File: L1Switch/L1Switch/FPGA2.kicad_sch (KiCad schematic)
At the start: 43 parts, among them J10 Conn_02x07_Odd_Even, U1 XC7A35T-FTG256, U10 W25Q128JVS, U11 TXB0108PW, U12 TPS386000RGPR

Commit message: Update part numbers.
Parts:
- C376, C377: MFR Part# GRM155R71C104KA57D -> GRM155R71C104KA88D
- R256, R257, R258: MFR Part# (none) -> RC0402FR-132KL; Manufacturer (none) -> Yageo
- R259: MFR Part# (none) -> RC0402FR-074K7L; Manufacturer (none) -> Yageo
- R260: MFR Part# (none) -> RC0402FR-0768K1L; Manufacturer (none) -> Yageo
- R261, R263, R265, R268: MFR Part# (none) -> CRCW040210K0FKED; Manufacturer (none) -> Vishay
- R262: MFR Part# (none) -> RC0402FR-0732K4L; Manufacturer (none) -> Yageo
- R264: MFR Part# (none) -> RC0402FR-0718K7L; Manufacturer (none) -> Yageo
- R266: MFR Part# (none) -> RC0402FR-0714K3L; Manufacturer (none) -> Yageo
- R267: MFR Part# (none) -> RC0402FR-071K1L; Manufacturer (none) -> Yageo
- R269: MFR Part# (none) -> RC0402FR-13100KL; Manufacturer (none) -> Yageo
- TP2, TP3, TP4: MFR Part# (none) -> -; Manufacturer (none) -> -
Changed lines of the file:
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@@
 (kicad_sch (version 20200608) (host eeschema "5.99.0-unknown-1973153~101~ubuntu20.04.1")
-  (page 3 12)
+  (page 1 12)
   (paper "B")
   (bus_alias "SPI_FLASH" (members "CS_N" "DI" "DO" "W_N" "HOLD_N"))
@@
   (junction (at 392.43 207.01))
   (junction (at 394.97 52.07))
-  (no_connect (at 233.68 120.65))
-  (no_connect (at 316.23 182.88))
+  (no_connect (at 233.68 138.43))
   (no_connect (at 367.03 148.59))
-  (no_connect (at 233.68 138.43))
   (no_connect (at 254 39.37))
   (no_connect (at 316.23 168.91))
+  (no_connect (at 316.23 182.88))
   (no_connect (at 254 41.91))
   (no_connect (at 233.68 123.19))
+  (no_connect (at 233.68 120.65))
   (no_connect (at 233.68 135.89))
   (bus_entry (at 347.98 49.53) (size -2.54 -2.54))
@@
       (effects (font (size 1.27 1.27)) hide)
     )
+    (property "MFR Part#" "-" (id 4) (at 242.57 105.41 0)
+      (effects (font (size 1.27 1.27)) hide)
+    )
+    (property "Manufacturer" "-" (id 5) (at 242.57 105.41 0)
+      (effects (font (size 1.27 1.27)) hide)
+    )
   )
   (symbol (lib_id "Connector:TestPoint") (at 256.54 113.03 180) (unit 1)
@@
       (effects (font (size 1.27 1.27)) hide)
     )
+    (property "MFR Part#" "-" (id 4) (at 256.54 113.03 0)
+      (effects (font (size 1.27 1.27)) hide)
+    )
+    (property "Manufacturer" "-" (id 5) (at 256.54 113.03 0)
+      (effects (font (size 1.27 1.27)) hide)
+    )
   )
   (symbol (lib_id "Connector:TestPoint") (at 379.73 127 0) (unit 1)
@@
     )
     (property "Datasheet" "~" (id 3) (at 384.81 127 0)
+      (effects (font (size 1.27 1.27)) hide)
+    )
+    (property "MFR Part#" "-" (id 4) (at 379.73 127 0)
+      (effects (font (size 1.27 1.27)) hide)
+    )
+    (property "Manufacturer" "-" (id 5) (at 379.73 127 0)
       (effects (font (size 1.27 1.27)) hide)
     )
@@
       (effects (font (size 1.27 1.27)) hide)
     )
+    (property "MFR Part#" "RC0402FR-074K7L" (id 4) (at 278.13 110.49 0)
+      (effects (font (size 1.27 1.27)) hide)
+    )
+    (property "Manufacturer" "Yageo" (id 5) (at 278.13 110.49 0)
+      (effects (font (size 1.27 1.27)) hide)
+    )
   )
   (symbol (lib_id "Device:R_US") (at 278.13 144.78 0) (unit 1)
@@
       (effects (font (size 1.27 1.27)) hide)
     )
+    (property "MFR Part#" "RC0402FR-0768K1L" (id 4) (at 278.13 144.78 0)
+      (effects (font (size 1.27 1.27)) hide)
+    )
+    (property "Manufacturer" "Yageo" (id 5) (at 278.13 144.78 0)
+      (effects (font (size 1.27 1.27)) hide)
+    )
   )
   (symbol (lib_id "Device:R_US") (at 278.13 184.15 0) (unit 1)
@@
       (effects (font (size 1.27 1.27)) hide)
     )
+    (property "MFR Part#" "CRCW040210K0FKED" (id 4) (at 278.13 184.15 0)
+      (effects (font (size 1.27 1.27)) hide)
+    )
+    (property "Manufacturer" "Vishay" (id 5) (at 278.13 184.15 0)
+      (effects (font (size 1.27 1.27)) hide)
+    )
   )
   (symbol (lib_id "Device:R_US") (at 288.29 144.78 0) (unit 1)
@@
       (effects (font (size 1.27 1.27)) hide)
     )
+    (property "MFR Part#" "RC0402FR-0732K4L" (id 4) (at 288.29 144.78 0)
+      (effects (font (size 1.27 1.27)) hide)
+    )
+    (property "Manufacturer" "Yageo" (id 5) (at 288.29 144.78 0)
+      (effects (font (size 1.27 1.27)) hide)
+    )
   )
   (symbol (lib_id "Device:R_US") (at 288.29 184.15 0) (unit 1)
@@
       (effects (font (size 1.27 1.27)) hide)
     )
+    (property "MFR Part#" "CRCW040210K0FKED" (id 4) (at 288.29 184.15 0)
+      (effects (font (size 1.27 1.27)) hide)
+    )
+    (property "Manufacturer" "Vishay" (id 5) (at 288.29 184.15 0)
+      (effects (font (size 1.27 1.27)) hide)
+    )
   )
   (symbol (lib_id "Device:R_US") (at 297.18 144.78 0) (unit 1)
@@
       (effects (font (size 1.27 1.27)) hide)
     )
+    (property "MFR Part#" "RC0402FR-0718K7L" (id 4) (at 297.18 144.78 0)
+      (effects (font (size 1.27 1.27)) hide)
+    )
+    (property "Manufacturer" "Yageo" (id 5) (at 297.18 144.78 0)
+      (effects (font (size 1.27 1.27)) hide)
+    )
   )
   (symbol (lib_id "Device:R_US") (at 297.18 184.15 0) (unit 1)
@@
       (effects (font (size 1.27 1.27)) hide)
     )
+    (property "MFR Part#" "CRCW040210K0FKED" (id 4) (at 297.18 184.15 0)
+      (effects (font (size 1.27 1.27)) hide)
+    )
+    (property "Manufacturer" "Vishay" (id 5) (at 297.18 184.15 0)
+      (effects (font (size 1.27 1.27)) hide)
+    )
   )
   (symbol (lib_id "Device:R_US") (at 306.07 144.78 0) (unit 1)
@@
       (effects (font (size 1.27 1.27)) hide)
     )
+    (property "MFR Part#" "RC0402FR-0714K3L" (id 4) (at 306.07 144.78 0)
+      (effects (font (size 1.27 1.27)) hide)
+    )
+    (property "Manufacturer" "Yageo" (id 5) (at 306.07 144.78 0)
+      (effects (font (size 1.27 1.27)) hide)
+    )
   )
   (symbol (lib_id "Device:R_US") (at 306.07 167.64 0) (unit 1)
@@
       (effects (font (size 1.27 1.27)) hide)
     )
+    (property "MFR Part#" "RC0402FR-071K1L" (id 4) (at 306.07 167.64 0)
+      (effects (font (size 1.27 1.27)) hide)
+    )
+    (property "Manufacturer" "Yageo" (id 5) (at 306.07 167.64 0)
+      (effects (font (size 1.27 1.27)) hide)
+    )
   )
   (symbol (lib_id "Device:R_US") (at 306.07 184.15 0) (unit 1)
@@
       (effects (font (size 1.27 1.27)) hide)
     )
+    (property "MFR Part#" "CRCW040210K0FKED" (id 4) (at 306.07 184.15 0)
+      (effects (font (size 1.27 1.27)) hide)
+    )
+    (property "Manufacturer" "Vishay" (id 5) (at 306.07 184.15 0)
+      (effects (font (size 1.27 1.27)) hide)
+    )
   )
   (symbol (lib_id "Device:R_US") (at 307.34 116.84 0) (unit 1)
@@
       (effects (font (size 1.27 1.27)) hide)
     )
+    (property "MFR Part#" "RC0402FR-13100KL" (id 4) (at 307.34 116.84 0)
+      (effects (font (size 1.27 1.27)) hide)
+    )
+    (property "Manufacturer" "Yageo" (id 5) (at 307.34 116.84 0)
+      (effects (font (size 1.27 1.27)) hide)
+    )
   )
   (symbol (lib_id "Device:R_US") (at 355.6 40.64 0) (unit 1)
@@
       (effects (font (size 1.27 1.27)) hide)
     )
+    (property "MFR Part#" "RC0402FR-132KL" (id 4) (at 355.6 40.64 0)
+      (effects (font (size 1.27 1.27)) hide)
+    )
+    (property "Manufacturer" "Yageo" (id 5) (at 355.6 40.64 0)
+      (effects (font (size 1.27 1.27)) hide)
+    )
   )
   (symbol (lib_id "Device:R_US") (at 387.35 39.37 0) (unit 1)
@@
       (effects (font (size 1.27 1.27)) hide)
     )
+    (property "MFR Part#" "RC0402FR-132KL" (id 4) (at 387.35 39.37 0)
+      (effects (font (size 1.27 1.27)) hide)
+    )
+    (property "Manufacturer" "Yageo" (id 5) (at 387.35 39.37 0)
+      (effects (font (size 1.27 1.27)) hide)
+    )
   )
   (symbol (lib_id "Device:R_US") (at 394.97 39.37 0) (unit 1)
@@
     )
     (property "Datasheet" "~" (id 3) (at 394.97 39.37 0)
+      (effects (font (size 1.27 1.27)) hide)
+    )
+    (property "MFR Part#" "RC0402FR-132KL" (id 4) (at 394.97 39.37 0)
+      (effects (font (size 1.27 1.27)) hide)
+    )
+    (property "Manufacturer" "Yageo" (id 5) (at 394.97 39.37 0)
       (effects (font (size 1.27 1.27)) hide)
     )
@@
       (effects (font (size 1.27 1.27)) hide)
     )
-    (property "MFR Part#" "GRM155R71C104KA57D" (id 4) (at 364.49 31.75 0)
+    (property "MFR Part#" "GRM155R71C104KA88D" (id 4) (at 364.49 31.75 0)
       (effects (font (size 1.27 1.27)) hide)
     )
@@
       (effects (font (size 1.27 1.27)) hide)
     )
-    (property "MFR Part#" "GRM155R71C104KA57D" (id 4) (at 386.08 31.75 0)
-      (effects (font (size 1.27 1.27)) hide)
-    )
+    (property "MFR Part#" "GRM155R71C104KA88D" (id 4) (at 386.08 31.75 0)
+      (effects (font (size 1.27 1.27)) hide)
+    )

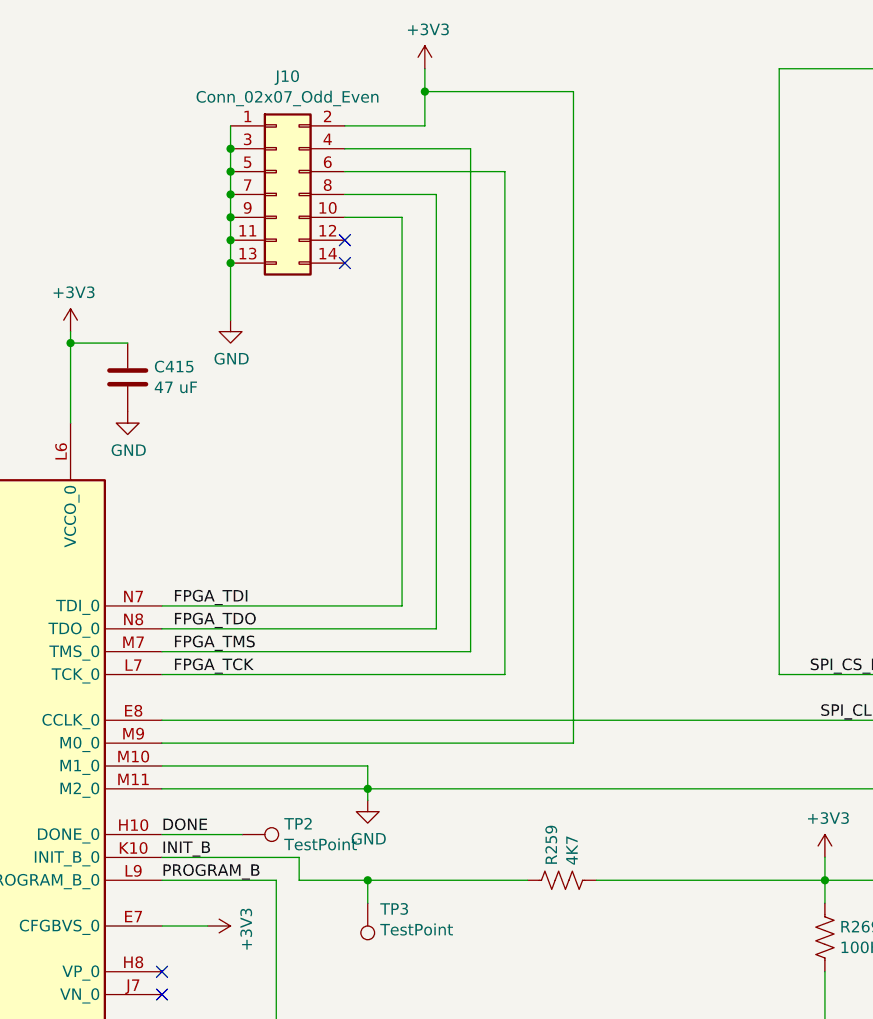
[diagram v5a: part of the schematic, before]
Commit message: Swap fan connector orientation. Add PU/PD for JTAG pins.
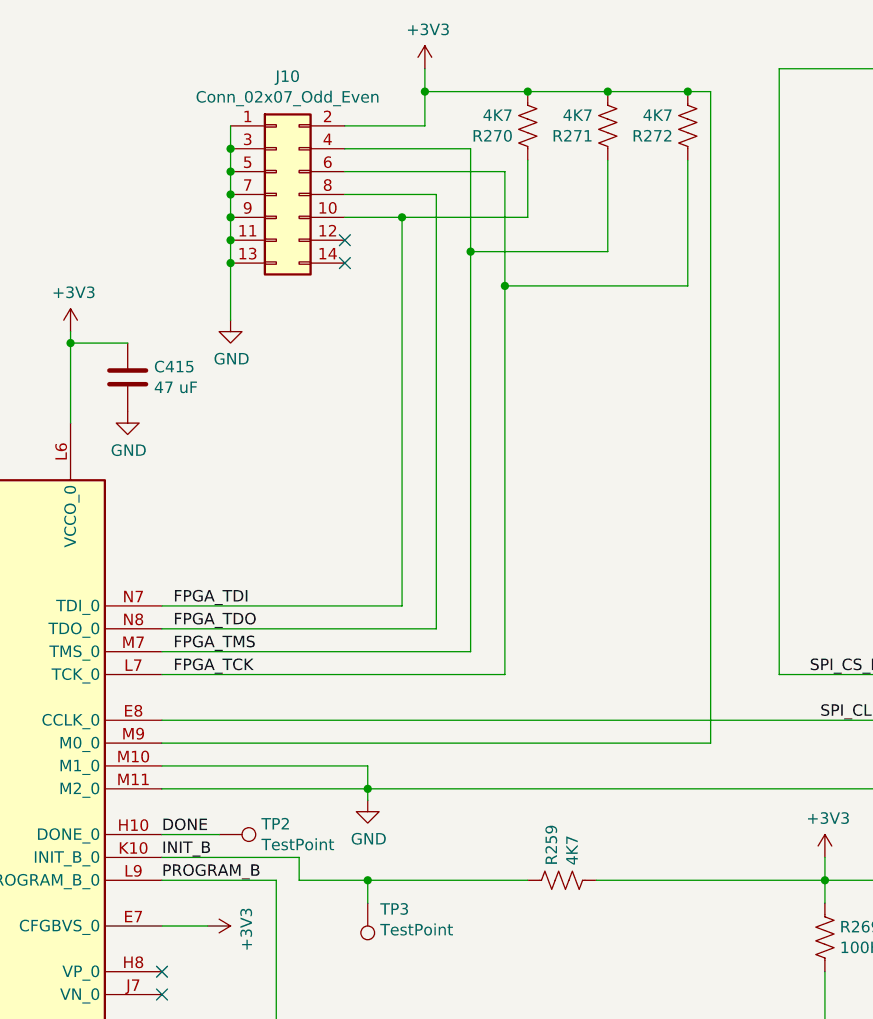
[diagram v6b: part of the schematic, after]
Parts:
- added R270, R271, R272: 4K7, Resistor_SMD:R_0402_1005Metric, symbol Device:R_US
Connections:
- net +3V3: now also R270.2, R271.2, R272.2
- net FPGA_TCK: now also R272.1
- net FPGA_TDI: now also R270.1
- net FPGA_TMS: now also R271.1
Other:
- moved on the sheet: TP2
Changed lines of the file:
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@@
 (kicad_sch (version 20200608) (host eeschema "5.99.0-unknown-1973153~101~ubuntu20.04.1")
-  (page 1 12)
+  (page 3 12)
   (paper "B")
   (bus_alias "SPI_FLASH" (members "CS_N" "DI" "DO" "W_N" "HOLD_N"))
@@
   (junction (at 257.81 190.5))
   (junction (at 257.81 200.66))
+  (junction (at 260.35 36.83))
   (junction (at 262.89 22.86))
+  (junction (at 267.97 40.64))
+  (junction (at 271.78 44.45))
+  (junction (at 274.32 22.86))
   (junction (at 278.13 153.67))
+  (junction (at 283.21 22.86))
   (junction (at 288.29 156.21))
   (junction (at 288.29 193.04))
+  (junction (at 292.1 22.86))
   (junction (at 297.18 158.75))
   (junction (at 297.18 193.04))
@@
   (junction (at 392.43 207.01))
   (junction (at 394.97 52.07))
+  (no_connect (at 254 41.91))
+  (no_connect (at 316.23 182.88))
   (no_connect (at 233.68 120.65))
   (no_connect (at 233.68 135.89))
+  (no_connect (at 254 39.37))
   (no_connect (at 233.68 138.43))
-  (no_connect (at 254 39.37))
-  (no_connect (at 254 41.91))
-  (no_connect (at 316.23 182.88))
   (no_connect (at 233.68 123.19))
+  (no_connect (at 316.23 168.91))
   (no_connect (at 367.03 148.59))
-  (no_connect (at 316.23 168.91))
   (bus_entry (at 347.98 49.53) (size -2.54 -2.54))
   (bus_entry (at 347.98 52.07) (size -2.54 -2.54))
@@
     (stroke (width 0) (type solid) (color 0 0 0 0))
   )
-  (wire (pts (xy 233.68 95.25) (xy 279.4 95.25))
+  (wire (pts (xy 233.68 95.25) (xy 294.64 95.25))
     (stroke (width 0) (type solid) (color 0 0 0 0))
   )
@@
     (stroke (width 0) (type solid) (color 0 0 0 0))
   )
-  (wire (pts (xy 233.68 105.41) (xy 242.57 105.41))
+  (wire (pts (xy 233.68 105.41) (xy 240.03 105.41))
     (stroke (width 0) (type solid) (color 0 0 0 0))
   )
@@
     (stroke (width 0) (type solid) (color 0 0 0 0))
   )
+  (wire (pts (xy 260.35 36.83) (xy 274.32 36.83))
+    (stroke (width 0) (type solid) (color 0 0 0 0))
+  )
   (wire (pts (xy 260.35 80.01) (xy 260.35 36.83))
     (stroke (width 0) (type solid) (color 0 0 0 0))
@@
     (stroke (width 0) (type solid) (color 0 0 0 0))
   )
-  (wire (pts (xy 267.97 85.09) (xy 267.97 29.21))
+  (wire (pts (xy 267.97 40.64) (xy 267.97 29.21))
+    (stroke (width 0) (type solid) (color 0 0 0 0))
+  )
+  (wire (pts (xy 267.97 40.64) (xy 283.21 40.64))
+    (stroke (width 0) (type solid) (color 0 0 0 0))
+  )
+  (wire (pts (xy 267.97 85.09) (xy 267.97 40.64))
     (stroke (width 0) (type solid) (color 0 0 0 0))
   )
@@
     (stroke (width 0) (type solid) (color 0 0 0 0))
   )
-  (wire (pts (xy 271.78 31.75) (xy 271.78 87.63))
+  (wire (pts (xy 271.78 31.75) (xy 271.78 44.45))
+    (stroke (width 0) (type solid) (color 0 0 0 0))
+  )
+  (wire (pts (xy 271.78 44.45) (xy 271.78 87.63))
+    (stroke (width 0) (type solid) (color 0 0 0 0))
+  )
+  (wire (pts (xy 271.78 44.45) (xy 292.1 44.45))
+    (stroke (width 0) (type solid) (color 0 0 0 0))
+  )
+  (wire (pts (xy 274.32 22.86) (xy 262.89 22.86))
+    (stroke (width 0) (type solid) (color 0 0 0 0))
+  )
+  (wire (pts (xy 274.32 36.83) (xy 274.32 30.48))
     (stroke (width 0) (type solid) (color 0 0 0 0))
   )
@@
     (stroke (width 0) (type solid) (color 0 0 0 0))
   )
-  (wire (pts (xy 279.4 22.86) (xy 262.89 22.86))
-    (stroke (width 0) (type solid) (color 0 0 0 0))
-  )
-  (wire (pts (xy 279.4 95.25) (xy 279.4 22.86))
-    (stroke (width 0) (type solid) (color 0 0 0 0))
-  )
   (wire (pts (xy 281.94 110.49) (xy 307.34 110.49))
     (stroke (width 0) (type solid) (color 0 0 0 0))
   )
+  (wire (pts (xy 283.21 22.86) (xy 274.32 22.86))
+    (stroke (width 0) (type solid) (color 0 0 0 0))
+  )
+  (wire (pts (xy 283.21 40.64) (xy 283.21 30.48))
+    (stroke (width 0) (type solid) (color 0 0 0 0))
+  )
   (wire (pts (xy 288.29 135.89) (xy 288.29 140.97))
     (stroke (width 0) (type solid) (color 0 0 0 0))
@@
   )
   (wire (pts (xy 288.29 193.04) (xy 297.18 193.04))
+    (stroke (width 0) (type solid) (color 0 0 0 0))
+  )
+  (wire (pts (xy 292.1 22.86) (xy 283.21 22.86))
+    (stroke (width 0) (type solid) (color 0 0 0 0))
+  )
+  (wire (pts (xy 292.1 44.45) (xy 292.1 30.48))
+    (stroke (width 0) (type solid) (color 0 0 0 0))
+  )
+  (wire (pts (xy 294.64 22.86) (xy 292.1 22.86))
+    (stroke (width 0) (type solid) (color 0 0 0 0))
+  )
+  (wire (pts (xy 294.64 95.25) (xy 294.64 22.86))
     (stroke (width 0) (type solid) (color 0 0 0 0))
   )
@@
     (effects (font (size 1.27 1.27)) (justify left))
   )
-  (symbol (lib_id "Connector:TestPoint") (at 242.57 105.41 270) (unit 1)
-    (in_bom yes) (on_board yes)
-    (property "Reference" "TP2" (id 0) (at 247.2691 104.2606 90)
-      (effects (font (size 1.27 1.27)) (justify left))
-    )
-    (property "Value" "TestPoint" (id 1) (at 247.2691 106.5593 90)
-      (effects (font (size 1.27 1.27)) (justify left))
-    )
-    (property "Footprint" "TestPoint:TestPoint_Pad_1.0x1.0mm" (id 2) (at 242.57 110.49 0)
-      (effects (font (size 1.27 1.27)) hide)
-    )
-    (property "Datasheet" "~" (id 3) (at 242.57 110.49 0)
-      (effects (font (size 1.27 1.27)) hide)
-    )
-    (property "MFR Part#" "-" (id 4) (at 242.57 105.41 0)
-      (effects (font (size 1.27 1.27)) hide)
-    )
-    (property "Manufacturer" "-" (id 5) (at 242.57 105.41 0)
+  (symbol (lib_id "Connector:TestPoint") (at 240.03 105.41 270) (unit 1)
+    (in_bom yes) (on_board yes)
+    (property "Reference" "TP2" (id 0) (at 244.7291 104.2606 90)
+      (effects (font (size 1.27 1.27)) (justify left))
+    )
+    (property "Value" "TestPoint" (id 1) (at 244.7291 106.5593 90)
+      (effects (font (size 1.27 1.27)) (justify left))
+    )
+    (property "Footprint" "TestPoint:TestPoint_Pad_1.0x1.0mm" (id 2) (at 240.03 110.49 0)
+      (effects (font (size 1.27 1.27)) hide)
+    )
+    (property "Datasheet" "~" (id 3) (at 240.03 110.49 0)
+      (effects (font (size 1.27 1.27)) hide)
+    )
+    (property "MFR Part#" "-" (id 4) (at 240.03 105.41 0)
+      (effects (font (size 1.27 1.27)) hide)
+    )
+    (property "Manufacturer" "-" (id 5) (at 240.03 105.41 0)
       (effects (font (size 1.27 1.27)) hide)
     )
@@
     )
   )
+  (symbol (lib_id "Device:R_US") (at 274.32 26.67 180) (unit 1)
+    (in_bom yes) (on_board yes)
+    (property "Reference" "R270" (id 0) (at 272.6689 27.8194 0)
+      (effects (font (size 1.27 1.27)) (justify left))
+    )
+    (property "Value" "4K7" (id 1) (at 272.6689 25.5207 0)
+      (effects (font (size 1.27 1.27)) (justify left))
+    )
+    (property "Footprint" "Resistor_SMD:R_0402_1005Metric" (id 2) (at 273.304 26.416 90)
+      (effects (font (size 1.27 1.27)) hide)
+    )
+    (property "Datasheet" "~" (id 3) (at 274.32 26.67 0)
+      (effects (font (size 1.27 1.27)) hide)
+    )
+    (property "MFR Part#" "RC0402FR-074K7L" (id 4) (at 274.32 26.67 0)
+      (effects (font (size 1.27 1.27)) hide)
+    )
+    (property "Manufacturer" "Yageo" (id 5) (at 274.32 26.67 0)
+      (effects (font (size 1.27 1.27)) hide)
+    )
+  )
   (symbol (lib_id "Device:R_US") (at 278.13 110.49 90) (unit 1)
     (in_bom yes) (on_board yes)
@@
     )
   )
+  (symbol (lib_id "Device:R_US") (at 283.21 26.67 180) (unit 1)
+    (in_bom yes) (on_board yes)
+    (property "Reference" "R271" (id 0) (at 281.5589 27.8194 0)
+      (effects (font (size 1.27 1.27)) (justify left))
+    )
+    (property "Value" "4K7" (id 1) (at 281.5589 25.5207 0)
+      (effects (font (size 1.27 1.27)) (justify left))
+    )
+    (property "Footprint" "Resistor_SMD:R_0402_1005Metric" (id 2) (at 282.194 26.416 90)
+      (effects (font (size 1.27 1.27)) hide)
+    )
+    (property "Datasheet" "~" (id 3) (at 283.21 26.67 0)
+      (effects (font (size 1.27 1.27)) hide)
+    )
+    (property "MFR Part#" "RC0402FR-074K7L" (id 4) (at 283.21 26.67 0)
+      (effects (font (size 1.27 1.27)) hide)
+    )
+    (property "Manufacturer" "Yageo" (id 5) (at 283.21 26.67 0)
+      (effects (font (size 1.27 1.27)) hide)
+    )
+  )
   (symbol (lib_id "Device:R_US") (at 288.29 144.78 0) (unit 1)
     (in_bom yes) (on_board yes)
@@
       (effects (font (size 1.27 1.27)) hide)
     )
+  )
+  (symbol (lib_id "Device:R_US") (at 292.1 26.67 180) (unit 1)
+    (in_bom yes) (on_board yes)
+    (property "Reference" "R272" (id 0) (at 290.4489 27.8194 0)
+      (effects (font (size 1.27 1.27)) (justify left))
+    )
+    (property "Value" "4K7" (id 1) (at 290.4489 25.5207 0)
+      (effects (font (size 1.27 1.27)) (justify left))
+    )
+    (property "Footprint" "Resistor_SMD:R_0402_1005Metric" (id 2) (at 291.084 26.416 90)
+      (effects (font (size 1.27 1.27)) hide)
+    )
+    (property "Datasheet" "~" (id 3) (at 292.1 26.67 0)
+      (effects (font (size 1.27 1.27)) hide)
+    )
+    (property "MFR Part#" "RC0402FR-074K7L" (id 4) (at 292.1 26.67 0)
+      (effects (font (size 1.27 1.27)) hide)
+    )
+    (property "Manufacturer" "Yageo" (id 5) (at 292.1 26.67 0)
+      (effects (font (size 1.27 1.27)) hide)
+    )
